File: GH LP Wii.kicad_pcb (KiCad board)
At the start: 2 copper layers, 6 parts

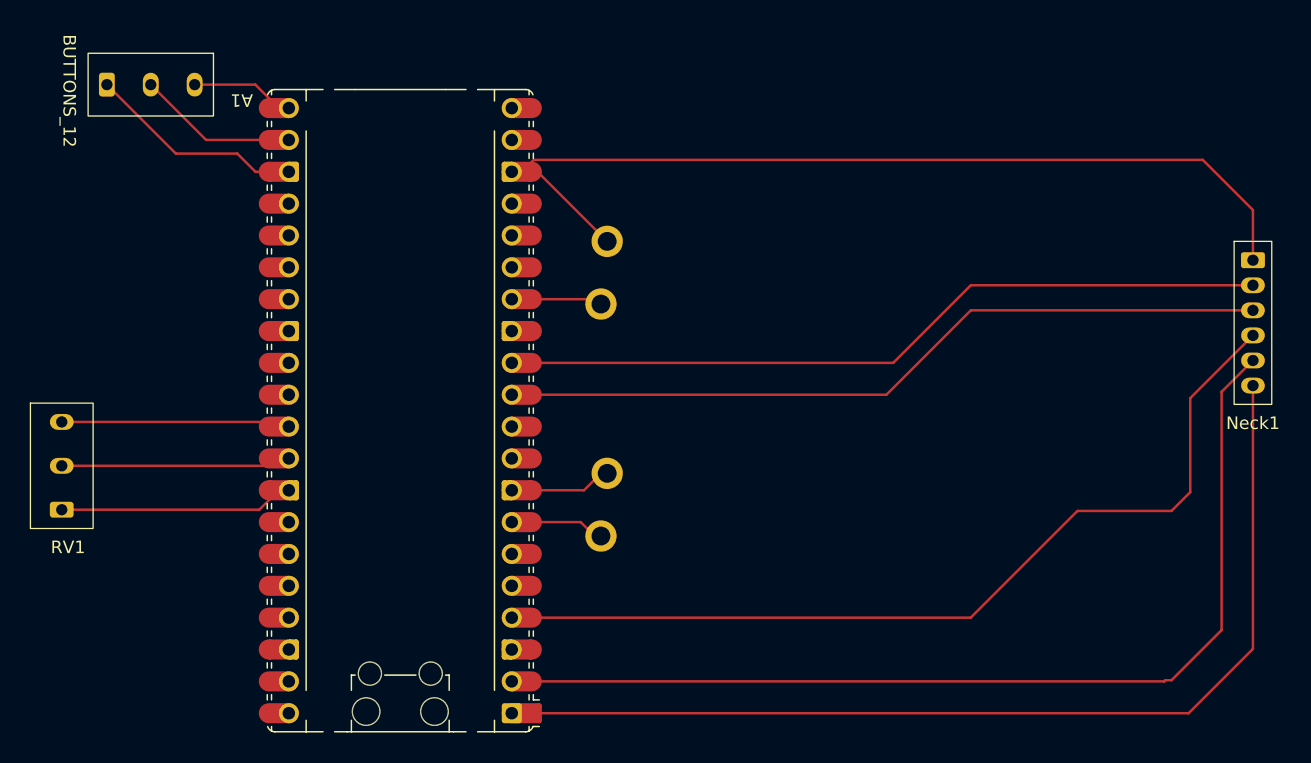
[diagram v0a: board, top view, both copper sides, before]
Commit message: add edge cuts
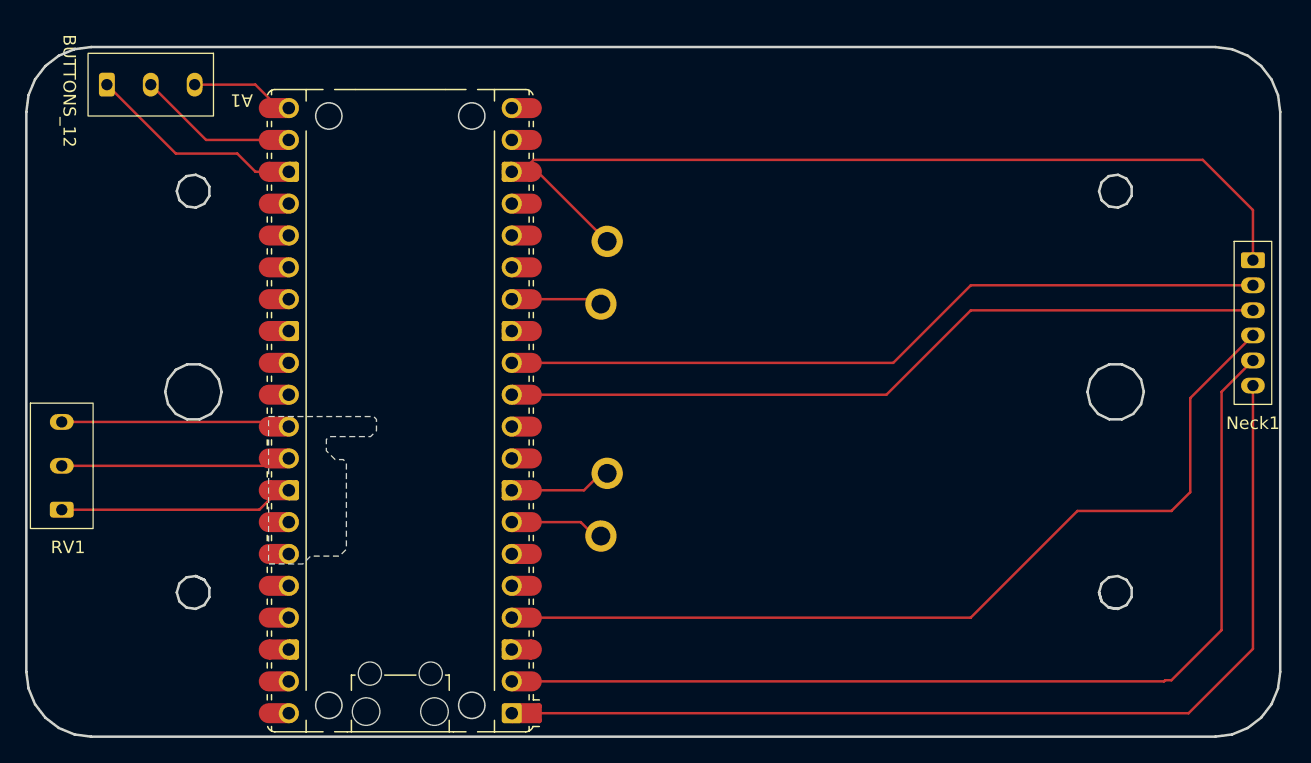
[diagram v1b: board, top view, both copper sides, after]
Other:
- board outline added: 100 x 55 mm

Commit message: gonna print
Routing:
- net Net-(Neck1-GND): track 97.4 -> 117.2 mm
- net Net-(A1-AGND): track 18.0 -> 16.6 mm
- net Net-(A1-GPIO26_ADC0): track 17.5 -> 16.7 mm

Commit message: Update settings and stuff
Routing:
- net Net-(Neck1-GND): track 117.2 -> 127.8 mm
